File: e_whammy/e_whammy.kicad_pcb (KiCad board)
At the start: 4 copper layers, 30 x 12 mm, 17 parts, among them J1 I/O connector, U1 HT7550-1, U2 TLV6001UIDBVR, U3 DRV5056

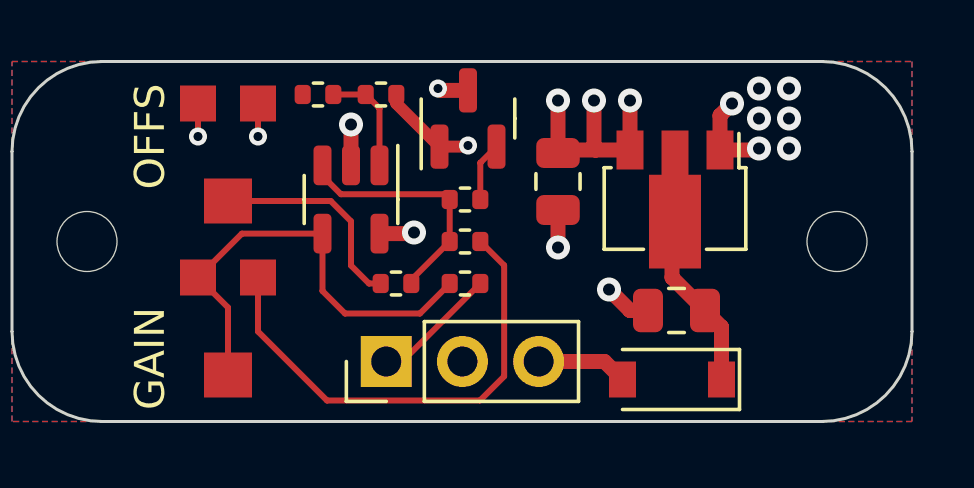
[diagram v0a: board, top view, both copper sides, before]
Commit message: Changed to non-inverting configuration
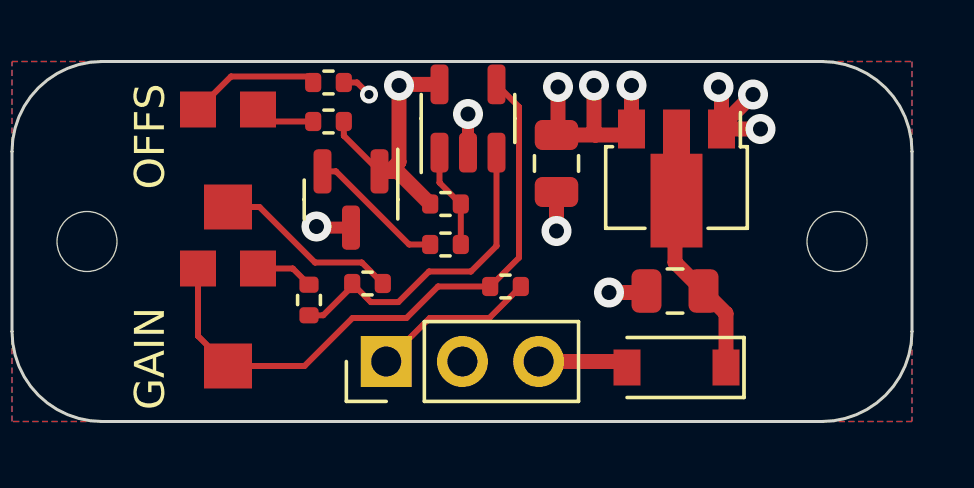
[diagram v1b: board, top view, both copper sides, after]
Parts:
- added R7: 1K, Resistor_SMD:R_0402_1005Metric, F.Cu at (141.4, 111.5)
- R1: value 10K -> 2K
- R2: value 1K -> 4.7K
- R6: value 10K -> 47K
- RV1: value TC33X-2-103E -> 2K
- U2: value TLV6001UIDBVR -> DRV5056; footprint Package_TO_SOT_SMD:SOT-23-5 -> Package_TO_SOT_SMD:SOT-23
- U3: value DRV5056 -> TLV6001UIDBVR; footprint Package_TO_SOT_SMD:SOT-23 -> Package_TO_SOT_SMD:SOT-23-5
- moved R2 8.10 mm to (135.6, 104.7), turned to 180 degrees
- moved R4 6.32 mm to (136.8, 111.4), turned to 180 degrees
- moved R1 5.85 mm to (135.6, 106.0)
- moved R5 5.60 mm to (139.4, 108.8), turned to 180 degrees
- moved R6 5.55 mm to (134.9, 112.0), turned to 90 degrees
- moved R3 1.63 mm to (139.4, 110.1), turned to 0 degrees
- moved U1 0.70 mm to (147.2, 107.9)
- moved C1 0.65 mm to (147.1, 111.7)
- moved C2 0.60 mm to (143.2, 107.4)
- moved D1 0.43 mm to (147.2, 114.2)
- moved RV2 0.30 mm to (132.2, 112.7)
- moved RV1 0.20 mm to (132.2, 107.4)
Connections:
- R1 pad 2: Net-(R1-Pad2) -> 5v
- R2 pad 1: Net-(R2-Pad1) -> GND
- R2 pad 2: OUT -> Net-(R2-Pad2)
- R3 pad 2: Net-(R1-Pad2) -> Net-(R3-Pad2)
- R4 pad 1: VREF -> Net-(R4-Pad1)
- R4 pad 2: 5v -> Net-(R4-Pad2)
- R5 pad 1: GND -> Net-(R3-Pad2)
- R5 pad 2: VREF -> 5v
- R6 pad 1: Net-(R1-Pad2) -> Net-(R4-Pad2)
- RV1 pad 1: GND -> Net-(R1-Pad1)
- RV1 pad 2: Net-(R1-Pad1) -> Net-(R4-Pad1)
- RV1 pad 3: 5v -> Net-(R2-Pad2)
- RV2 pad 2: Net-(R2-Pad1) -> Net-(R7-Pad1)
- RV2 pad 3: Net-(R2-Pad1) -> Net-(R7-Pad1)
- U2 pad 1: VREF -> 5v
- U2 pad 2: GND -> Net-(R3-Pad1)
- U2 pad 3: Net-(R1-Pad2) -> GND
- U3 pad 1: 5v -> Net-(R3-Pad2)
- U3 pad 2: Net-(R3-Pad1) -> GND
- U3 pad 3: GND -> Net-(R4-Pad2)
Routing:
- net Net-(R7-Pad1): track 0.00 -> 20.9 mm
- net Net-(R2-Pad1): track 15.3 -> 0.00 mm
- net Net-(R6-Pad2): track 16.1 -> 1.92 mm
- net Net-(R4-Pad2): track 0.00 -> 10.9 mm
- net Net-(R1-Pad2): track 8.25 -> 0.00 mm
- net Net-(R4-Pad1): track 0.00 -> 6.22 mm
- net Net-(R1-Pad1): track 7.09 -> 2.01 mm
- net Net-(R2-Pad2): track 0.00 -> 4.38 mm
- net VREF: track 3.63 -> 0.00 mm
- net Net-(R3-Pad2): track 0.00 -> 3.36 mm
- net 5v: track 13.1 -> 16.3 mm, vias 6 -> 4
- net Net-(R3-Pad1): track 1.99 -> 4.60 mm
- net OUT: track 4.21 -> 5.52 mm
- net GND: track 9.36 -> 10.4 mm, vias 12 -> 8

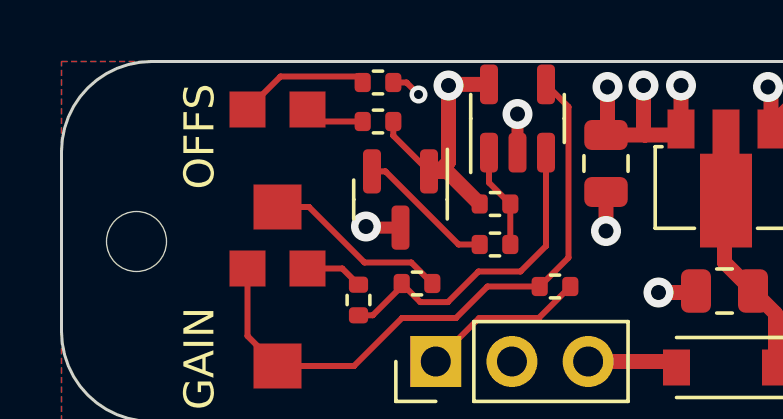
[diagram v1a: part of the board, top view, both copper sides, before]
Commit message: Adjusted values for component availability
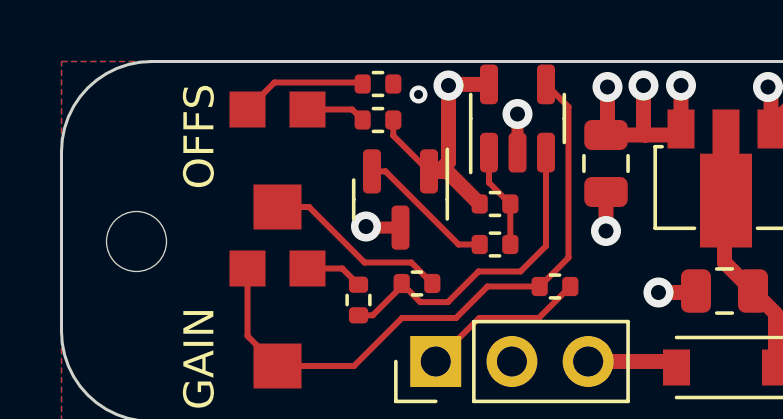
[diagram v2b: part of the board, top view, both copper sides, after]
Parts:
- R1: value 2K -> 10K
- R6: value 47K -> 100K
- RV1: value 2K -> 5K
- RV2: value TC33X-2-104E -> 100K
- moved R1 1.25 mm to (135.6, 104.8), turned to 180 degrees
- moved R2 1.25 mm to (135.6, 106.0), turned to 0 degrees
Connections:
- R1 pad 1: Net-(R1-Pad1) -> GND
- R1 pad 2: 5v -> Net-(RV1-Pad3)
- R2 pad 1: GND -> Net-(RV1-Pad1)
- R2 pad 2: Net-(R2-Pad2) -> 5v
- RV1 pad 1: Net-(R1-Pad1) -> Net-(RV1-Pad1)
- RV1 pad 3: Net-(R2-Pad2) -> Net-(RV1-Pad3)
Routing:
- net Net-(R2-Pad2): track 4.38 -> 0.00 mm
- net Net-(RV1-Pad3): track 0.00 -> 4.23 mm
- net Net-(R1-Pad1): track 2.01 -> 0.00 mm
- net Net-(RV1-Pad1): track 0.00 -> 1.98 mm
- net GND: track 10.4 -> 9.35 mm
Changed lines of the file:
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@@
   (net 2 "GND")
   (net 3 "5v")
-  (net 4 "Net-(R1-Pad1)")
+  (net 4 "Net-(RV1-Pad3)")
   (net 5 "V+")
   (net 6 "OUT")
   (net 7 "Net-(R3-Pad1)")
   (net 8 "Net-(R6-Pad2)")
-  (net 9 "Net-(R2-Pad2)")
+  (net 9 "Net-(RV1-Pad1)")
   (net 10 "Net-(R3-Pad2)")
   (net 11 "Net-(R4-Pad1)")
@@
       (effects (font (size 1 1) (thickness 0.15)))
     )
-    (fp_text value "TC33X-2-104E" (at 0.4 3.9 180 unlocked) (layer "F.Fab")
+    (fp_text value "100K" (at 0.4 3.9 180 unlocked) (layer "F.Fab")
       (effects (font (size 1 1) (thickness 0.15)))
     )
@@
     (at 132.2 107.4 180)
     (property "JLCPCB_CORRECTION" "0;0;270")
-    (property "LCSC" "C720647")
+    (property "LCSC" "C719177")
     (property "Sheetfile" "File: e_whammy.kicad_sch")
     (property "Sheetname" "")
@@
       (effects (font (size 1 1) (thickness 0.15)))
     )
-    (fp_text value "2K" (at 0.4 3.9 180 unlocked) (layer "F.Fab")
+    (fp_text value "5K" (at 0.4 3.9 180 unlocked) (layer "F.Fab")
       (effects (font (size 1 1) (thickness 0.15)))
     )
     (fp_rect (start -1.7 -2.3) (end 1.7 2.5) (layer "F.CrtYd") (width 0.12) (fill none))
     (pad "1" smd rect (at -1 1.8 180) (size 1.2 1.2) (layers "F.Cu" "F.Paste" "F.Mask")
-      (net 4 "Net-(R1-Pad1)") (pinfunction "1") (pintype "passive"))
+      (net 9 "Net-(RV1-Pad1)") (pinfunction "1") (pintype "passive"))
     (pad "2" smd rect (at 0 -1.45 180) (size 1.6 1.5) (layers "F.Cu" "F.Paste" "F.Mask")
       (net 11 "Net-(R4-Pad1)") (pinfunction "2") (pintype "passive"))
     (pad "3" smd rect (at 1 1.8 180) (size 1.2 1.2) (layers "F.Cu" "F.Paste" "F.Mask")
-      (net 9 "Net-(R2-Pad2)") (pinfunction "3") (pintype "passive"))
+      (net 4 "Net-(RV1-Pad3)") (pinfunction "3") (pintype "passive"))
   )
   (footprint "Resistor_SMD:R_0402_1005Metric" (layer "F.Cu")
@@
   )
   (footprint "Resistor_SMD:R_0402_1005Metric" (layer "F.Cu")
-    (at 135.55 106)
+    (at 135.55 104.75 180)
     (descr "Resistor SMD 0402 (1005 Metric), square (rectangular) end terminal, IPC_7351 nominal, (Body size source: IPC-SM-782 page 72, https://www.pcb-3d.com/wordpress/wp-content/uploads/ipc-sm-782a_amendment_1_and_2.pdf), generated with kicad-footprint-generator")
     (tags "resistor")
-    (property "LCSC" "C4109")
+    (property "LCSC" "C25744")
     (property "Sheetfile" "File: e_whammy.kicad_sch")
     (property "Sheetname" "")
@@
       (effects (font (size 1 1) (thickness 0.15)))
     )
-    (fp_text value "2K" (at 0 1.17) (layer "F.Fab")
+    (fp_text value "10K" (at 0 1.17) (layer "F.Fab")
       (effects (font (size 1 1) (thickness 0.15)))
     )
@@
     (fp_line (start 0.525 0.27) (end -0.525 0.27) (layer "F.Fab") (width 0.1))
     (fp_line (start -0.525 0.27) (end -0.525 -0.27) (layer "F.Fab") (width 0.1))
-    (pad "1" smd roundrect (at -0.51 0) (size 0.54 0.64) (layers "F.Cu" "F.Paste" "F.Mask") (roundrect_rratio 0.25)
-      (net 4 "Net-(R1-Pad1)") (pintype "passive"))
-    (pad "2" smd roundrect (at 0.51 0) (size 0.54 0.64) (layers "F.Cu" "F.Paste" "F.Mask") (roundrect_rratio 0.25)
-      (net 3 "5v") (pintype "passive"))
+    (pad "1" smd roundrect (at -0.51 0 180) (size 0.54 0.64) (layers "F.Cu" "F.Paste" "F.Mask") (roundrect_rratio 0.25)
+      (net 2 "GND") (pintype "passive"))
+    (pad "2" smd roundrect (at 0.51 0 180) (size 0.54 0.64) (layers "F.Cu" "F.Paste" "F.Mask") (roundrect_rratio 0.25)
+      (net 4 "Net-(RV1-Pad3)") (pintype "passive"))
     (model "${KICAD6_3DMODEL_DIR}/Resistor_SMD.3dshapes/R_0402_1005Metric.wrl"
       (offset (xyz 0 0 0))
@@
   )
   (footprint "Resistor_SMD:R_0402_1005Metric" (layer "F.Cu")
-    (at 135.55 104.7 180)
+    (at 135.55 105.95)
     (descr "Resistor SMD 0402 (1005 Metric), square (rectangular) end terminal, IPC_7351 nominal, (Body size source: IPC-SM-782 page 72, https://www.pcb-3d.com/wordpress/wp-content/uploads/ipc-sm-782a_amendment_1_and_2.pdf), generated with kicad-footprint-generator")
     (tags "resistor")
@@
     (fp_line (start -0.525 0.27) (end -0.525 -0.27) (layer "F.Fab") (width 0.1))
     (fp_line (start 0.525 -0.27) (end 0.525 0.27) (layer "F.Fab") (width 0.1))
-    (pad "1" smd roundrect (at -0.51 0 180) (size 0.54 0.64) (layers "F.Cu" "F.Paste" "F.Mask") (roundrect_rratio 0.25)
-      (net 2 "GND") (pintype "passive"))
-    (pad "2" smd roundrect (at 0.51 0 180) (size 0.54 0.64) (layers "F.Cu" "F.Paste" "F.Mask") (roundrect_rratio 0.25)
-      (net 9 "Net-(R2-Pad2)") (pintype "passive"))
+    (pad "1" smd roundrect (at -0.51 0) (size 0.54 0.64) (layers "F.Cu" "F.Paste" "F.Mask") (roundrect_rratio 0.25)
+      (net 9 "Net-(RV1-Pad1)") (pintype "passive"))
+    (pad "2" smd roundrect (at 0.51 0) (size 0.54 0.64) (layers "F.Cu" "F.Paste" "F.Mask") (roundrect_rratio 0.25)
+      (net 3 "5v") (pintype "passive"))
     (model "${KICAD6_3DMODEL_DIR}/Resistor_SMD.3dshapes/R_0402_1005Metric.wrl"
       (offset (xyz 0 0 0))
@@
     (descr "Resistor SMD 0402 (1005 Metric), square (rectangular) end terminal, IPC_7351 nominal, (Body size source: IPC-SM-782 page 72, https://www.pcb-3d.com/wordpress/wp-content/uploads/ipc-sm-782a_amendment_1_and_2.pdf), generated with kicad-footprint-generator")
     (tags "resistor")
-    (property "LCSC" "C25792")
+    (property "LCSC" "C25741")
     (property "Sheetfile" "File: e_whammy.kicad_sch")
     (property "Sheetname" "")
@@
       (effects (font (size 1 1) (thickness 0.15)))
     )
-    (fp_text value "47K" (at 0 1.17 90) (layer "F.Fab")
+    (fp_text value "100K" (at 0 1.17 90) (layer "F.Fab")
       (effects (font (size 1 1) (thickness 0.15)))
     )
@@
   (segment (start 148.8 112.4) (end 148.05 111.65) (width 0.5) (layer "F.Cu") (net 1))
   (segment (start 148.65 106.15) (end 149.7 105.1) (width 0.5) (layer "F.Cu") (net 2))
-  (segment (start 136.06 104.7) (end 136.5 104.7) (width 0.2) (layer "F.Cu") (net 2))
   (segment (start 148.65 106.25) (end 148.65 106.15) (width 0.5) (layer "F.Cu") (net 2))
   (segment (start 146.1 111.7) (end 144.9 111.7) (width 0.5) (layer "F.Cu") (net 2))
@@
   (segment (start 146.15 111.65) (end 146.1 111.7) (width 0.5) (layer "F.Cu") (net 2))
   (segment (start 136.3 109.5375) (end 135.1875 109.5375) (width 0.4) (layer "F.Cu") (net 2))
-  (segment (start 136.5 104.7) (end 136.9 105.1) (width 0.2) (layer "F.Cu") (net 2))
   (segment (start 135.1875 109.5375) (end 135.15 109.5) (width 0.4) (layer "F.Cu") (net 2))
   (segment (start 143.15 108.35) (end 143.15 109.65) (width 0.5) (layer "F.Cu") (net 2))
@@
   (segment (start 137.25 107.6625) (end 137.5875 107.6625) (width 0.5) (layer "F.Cu") (net 3))
   (segment (start 145.45 106.45) (end 144.45 106.45) (width 0.5) (layer "F.Cu") (net 3))
+  (segment (start 136.06 106.4725) (end 137.25 107.6625) (width 0.2) (layer "F.Cu") (net 3))
   (segment (start 143.15 106.45) (end 143.2 106.4) (width 0.5) (layer "F.Cu") (net 3))
   (segment (start 145.65 106.25) (end 145.45 106.45) (width 0.5) (layer "F.Cu") (net 3))
@@
   (segment (start 137.8525 107.6625) (end 138.94 108.75) (width 0.5) (layer "F.Cu") (net 3))
   (segment (start 144.4 106.4) (end 144.45 106.45) (width 0.5) (layer "F.Cu") (net 3))
+  (segment (start 136.06 105.95) (end 136.06 106.4725) (width 0.2) (layer "F.Cu") (net 3))
   (segment (start 137.9 107.35) (end 137.9 104.8) (width 0.5) (layer "F.Cu") (net 3))
   (segment (start 144.45 106.45) (end 143.15 106.45) (width 0.5) (layer "F.Cu") (net 3))
-  (segment (start 136.06 106) (end 136.06 106.4725) (width 0.2) (layer "F.Cu") (net 3))
-  (segment (start 136.06 106.4725) (end 137.25 107.6625) (width 0.2) (layer "F.Cu") (net 3))
   (via (at 137.9 104.8) (size 1) (drill 0.5) (layers "F.Cu" "B.Cu") (net 3))
   (via (at 143.2 104.85) (size 1) (drill 0.5) (layers "F.Cu" "B.Cu") (net 3))
   (via (at 145.65 104.8) (size 1) (drill 0.5) (layers "F.Cu" "B.Cu") (net 3))
   (via (at 144.4 104.8) (size 1) (drill 0.5) (layers "F.Cu" "B.Cu") (net 3))
-  (segment (start 133.2 105.6) (end 133.6 106) (width 0.2) (layer "F.Cu") (net 4))
-  (segment (start 133.6 106) (end 135.04 106) (width 0.2) (layer "F.Cu") (net 4))
+  (segment (start 132.1 104.7) (end 134.99 104.7) (width 0.2) (layer "F.Cu") (net 4))
+  (segment (start 134.99 104.7) (end 135.04 104.75) (width 0.2) (layer "F.Cu") (net 4))
+  (segment (start 131.2 105.6) (end 132.1 104.7) (width 0.2) (layer "F.Cu") (net 4))
   (segment (start 145.3 114) (end 145.5 114.2) (width 0.5) (layer "F.Cu") (net 5))
   (segment (start 142.555 114) (end 145.3 114) (width 0.5) (layer "F.Cu") (net 5))
@@
   (segment (start 134.36 110.9) (end 134.9 111.44) (width 0.2) (layer "F.Cu") (net 8))
   (segment (start 133.2 110.9) (end 134.36 110.9) (width 0.2) (layer "F.Cu") (net 8))
-  (segment (start 134.84 104.5) (end 135.04 104.7) (width 0.2) (layer "F.Cu") (net 9))
-  (segment (start 131.2 105.6) (end 132.3 104.5) (width 0.2) (layer "F.Cu") (net 9))
-  (segment (start 132.3 104.5) (end 134.84 104.5) (width 0.2) (layer "F.Cu") (net 9))
+  (segment (start 133.2 105.6) (end 134.69 105.6) (width 0.2) (layer "F.Cu") (net 9))
+  (segment (start 134.69 105.6) (end 135.04 105.95) (width 0.2) (layer "F.Cu") (net 9))
   (segment (start 139.25 107.0375) (end 139.25 108.04) (width 0.2) (layer "F.Cu") (net 10))
   (segment (start 139.25 108.04) (end 139.96 108.75) (width 0.2) (layer "F.Cu") (net 10))

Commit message: New uni-mount version
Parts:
- removed the REF** at (152.5, 110.0)
- removed the REF** at (127.5, 110.0)
- added REF**: hole_1.7mm, cycfi_library:hole_1.7mm, F.Cu at (123.0, 98.0)
- moved R7 30.2 mm to (111.4, 108.8), turned to 90 degrees
- moved U3 27.9 mm to (113.0, 111.8), turned to 180 degrees
- moved R2 26.0 mm to (111.1, 114.9), turned to 90 degrees
- moved R5 25.7 mm to (114.5, 114.9), turned to -90 degrees
- moved C2 24.9 mm to (119.3, 114.8), turned to 180 degrees
- moved R1 24.9 mm to (112.8, 114.9), turned to -90 degrees
- moved C1 24.2 mm to (123.1, 108.8), turned to 90 degrees
- moved J1 23.8 mm to (114.5, 107.7)
- moved R3 23.8 mm to (115.9, 113.5), turned to -90 degrees
- moved U1 23.7 mm to (124.1, 113.2), turned to 0 degrees
- moved D1 22.5 mm to (125.5, 108.2), turned to 90 degrees
- moved RV1 21.9 mm to (113.0, 117.8), turned to -90 degrees
- moved R4 21.0 mm to (115.9, 111.4), turned to 90 degrees
- moved R6 18.8 mm to (116.4, 115.3), turned to 0 degrees
- moved U2 18.2 mm to (118.4, 111.7)
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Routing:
- net GND: track 9.35 -> 0.00 mm, vias 8 -> 0
- net 5v: track 16.4 -> 9.59 mm, vias 4 -> 6
- net Net-(R6-Pad2): track 1.92 -> 6.17 mm
- net V+: track 3.03 -> 6.42 mm
- net OUT: track 5.52 -> 3.34 mm
- net Net-(U3--): track 10.9 -> 8.92 mm, vias 0 -> 2
- net Net-(D1-K): track 8.59 -> 6.79 mm
- net Net-(U2-OUT): track 4.60 -> 2.90 mm
- net Net-(R7-Pad1): track 20.9 -> 21.5 mm, vias 0 -> 2
- net Net-(R2-Pad1): track 1.98 -> 1.40 mm
- net Net-(R4-Pad1): track 6.22 -> 6.50 mm, vias 0 -> 2
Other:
- board size 30 x 12 mm -> 17 x 30 mm
